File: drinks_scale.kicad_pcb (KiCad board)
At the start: 2 copper layers, 62.2 x 34.3 mm, 4 parts, among them J1 CONN_01X02, J2 CONN_01X04, U1 hx711, U2 WeMos_mini

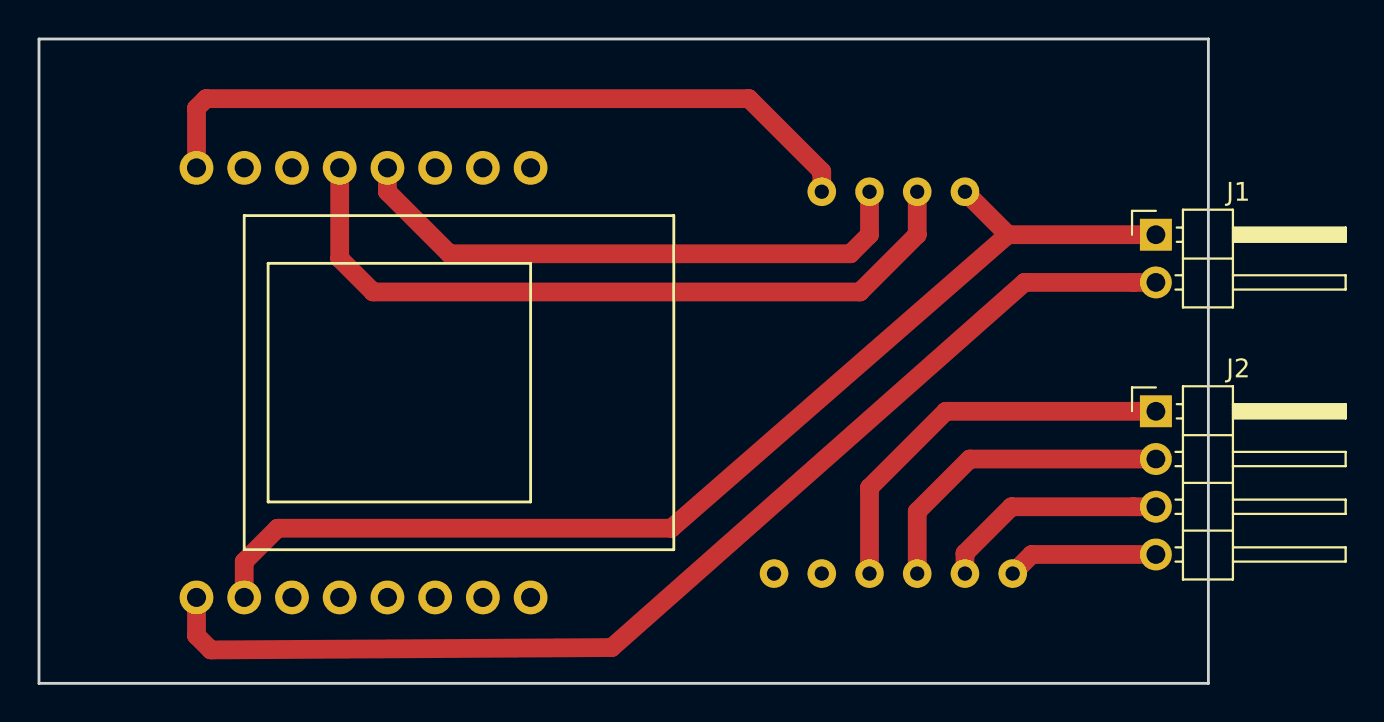
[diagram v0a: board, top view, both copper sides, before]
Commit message: Add GND plane
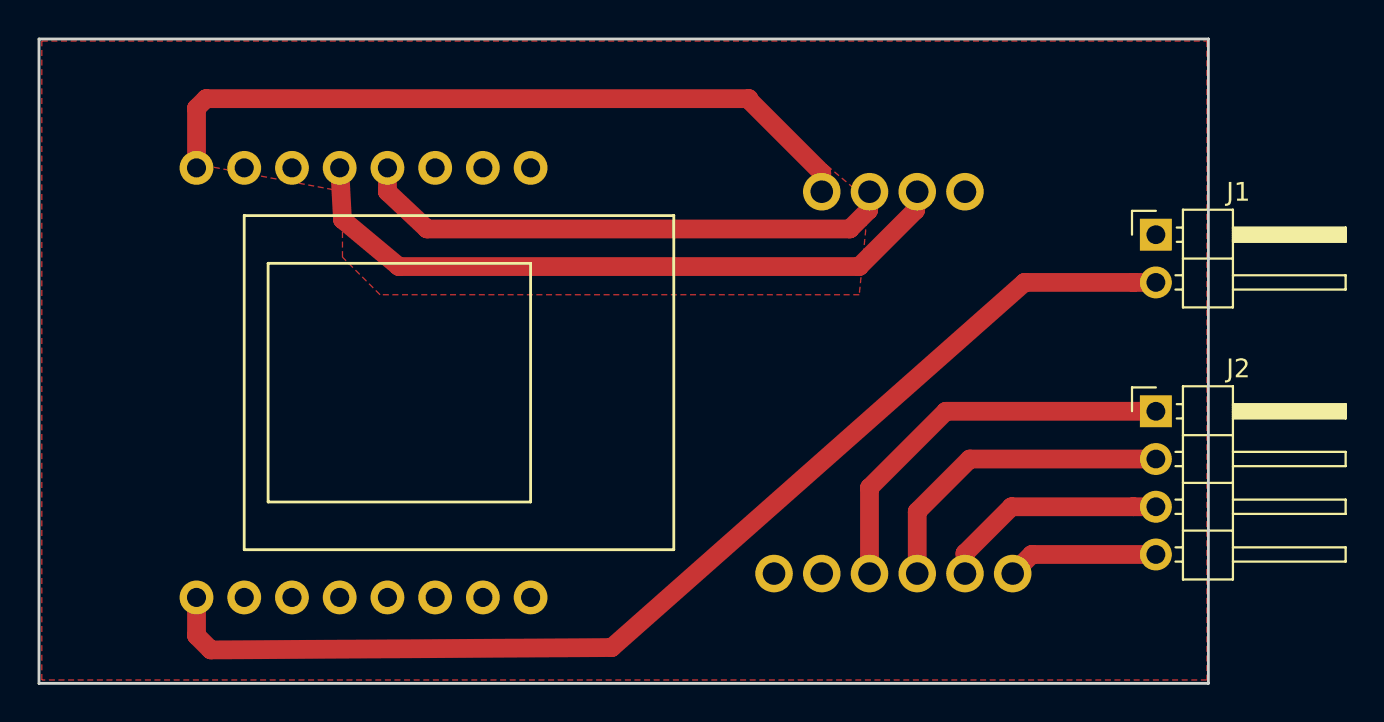
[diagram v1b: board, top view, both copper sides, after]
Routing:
- net GND: track 60.2 -> 0.00 mm
- net /data: track 39.8 -> 36.4 mm
- net /sck: track 31.0 -> 29.1 mm
- added copper zone on F.Cu, net (none)
- added copper zone on F.Cu, net GND
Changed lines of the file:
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@@
     (links 10)
     (no_connects 0)
-    (area 69.774999 72.314999 132.155001 106.755001)
+    (area 66.067 72.314999 140.061001 106.755001)
     (thickness 1.6)
     (drawings 4)
-    (tracks 39)
+    (tracks 34)
     (zones 0)
     (modules 4)
@@
     (trace_clearance 0.2)
     (zone_clearance 0.508)
-    (zone_45_only no)
+    (zone_45_only yes)
     (trace_min 0.2)
     (segment_width 0.2)
@@
     (fp_line (start -12.7 -10.16) (end 12.7 -10.16) (layer B.SilkS) (width 0.15))
     (fp_line (start -12.7 7.62) (end -12.7 -10.16) (layer B.SilkS) (width 0.15))
-    (pad 1 thru_hole circle (at -10.16 5.08 90) (size 1.524 1.524) (drill 0.762) (layers *.Cu *.Mask)
+    (pad 1 thru_hole circle (at -10.16 5.08 90) (size 2 2) (drill 1.2) (layers *.Cu *.Mask)
       (net 6 "Net-(J2-Pad4)"))
-    (pad 2 thru_hole circle (at -10.16 2.54 90) (size 1.524 1.524) (drill 0.762) (layers *.Cu *.Mask)
+    (pad 2 thru_hole circle (at -10.16 2.54 90) (size 2 2) (drill 1.2) (layers *.Cu *.Mask)
       (net 5 "Net-(J2-Pad3)"))
-    (pad 3 thru_hole circle (at -10.16 0 90) (size 1.524 1.524) (drill 0.762) (layers *.Cu *.Mask)
+    (pad 3 thru_hole circle (at -10.16 0 90) (size 2 2) (drill 1.2) (layers *.Cu *.Mask)
       (net 4 "Net-(J2-Pad2)"))
-    (pad 4 thru_hole circle (at -10.16 -2.54 90) (size 1.524 1.524) (drill 0.762) (layers *.Cu *.Mask)
+    (pad 4 thru_hole circle (at -10.16 -2.54 90) (size 2 2) (drill 1.2) (layers *.Cu *.Mask)
       (net 3 "Net-(J2-Pad1)"))
-    (pad 5 thru_hole circle (at -10.16 -5.08 90) (size 1.524 1.524) (drill 0.762) (layers *.Cu *.Mask))
-    (pad 6 thru_hole circle (at -10.16 -7.62 90) (size 1.524 1.524) (drill 0.762) (layers *.Cu *.Mask))
-    (pad 10 thru_hole circle (at 10.16 -5.08 90) (size 1.524 1.524) (drill 0.762) (layers *.Cu *.Mask)
+    (pad 5 thru_hole circle (at -10.16 -5.08 90) (size 2 2) (drill 1.2) (layers *.Cu *.Mask))
+    (pad 6 thru_hole circle (at -10.16 -7.62 90) (size 2 2) (drill 1.2) (layers *.Cu *.Mask))
+    (pad 10 thru_hole circle (at 10.16 -5.08 90) (size 2 2) (drill 1.2) (layers *.Cu *.Mask)
       (net 9 +3V3))
-    (pad 9 thru_hole circle (at 10.16 -2.54 90) (size 1.524 1.524) (drill 0.762) (layers *.Cu *.Mask)
+    (pad 9 thru_hole circle (at 10.16 -2.54 90) (size 2 2) (drill 1.2) (layers *.Cu *.Mask)
       (net 8 /sck))
-    (pad 8 thru_hole circle (at 10.16 0 90) (size 1.524 1.524) (drill 0.762) (layers *.Cu *.Mask)
+    (pad 8 thru_hole circle (at 10.16 0 90) (size 2 2) (drill 1.2) (layers *.Cu *.Mask)
       (net 7 /data))
-    (pad 7 thru_hole circle (at 10.16 2.54 90) (size 1.524 1.524) (drill 0.762) (layers *.Cu *.Mask)
+    (pad 7 thru_hole circle (at 10.16 2.54 90) (size 2 2) (drill 1.2) (layers *.Cu *.Mask)
       (net 1 GND))
   )
@@
   (gr_line (start 132.08 72.39) (end 132.08 106.68) (angle 90) (layer Edge.Cuts) (width 0.15))
   (gr_line (start 69.85 72.39) (end 132.08 72.39) (angle 90) (layer Edge.Cuts) (width 0.15))
-  (segment (start 121.412 82.804) (end 103.505 98.425) (width 1) (layer F.Cu) (net 1))
-  (segment (start 103.505 98.425) (end 82.55 98.425) (width 1) (layer F.Cu) (net 1))
-  (segment (start 82.55 98.425) (end 80.772 100.203) (width 1) (layer F.Cu) (net 1))
-  (segment (start 80.772 100.203) (end 80.772 102.108) (width 1) (layer F.Cu) (net 1))
-  (segment (start 119.126 80.518) (end 121.412 82.804) (width 1) (layer F.Cu) (net 1))
-  (segment (start 121.412 82.804) (end 129.286 82.804) (width 1) (layer F.Cu) (net 1))
   (segment (start 128.083919 85.344) (end 129.286 85.344) (width 1) (layer F.Cu) (net 2))
   (segment (start 78.232 102.108) (end 78.232 104.14) (width 1) (layer F.Cu) (net 2))
@@
   (segment (start 122.682 99.822) (end 129.286 99.822) (width 1) (layer F.Cu) (net 6))
   (segment (start 121.666 100.838) (end 122.682 99.822) (width 1) (layer F.Cu) (net 6))
-  (segment (start 85.852 79.248) (end 85.852 84.074) (width 1) (layer F.Cu) (net 7))
-  (segment (start 85.852 84.074) (end 87.63 85.852) (width 1) (layer F.Cu) (net 7))
-  (segment (start 87.63 85.852) (end 113.538 85.852) (width 1) (layer F.Cu) (net 7))
-  (segment (start 113.538 85.852) (end 116.586 82.804) (width 1) (layer F.Cu) (net 7))
-  (segment (start 116.586 82.804) (end 116.586 80.518) (width 1) (layer F.Cu) (net 7))
-  (segment (start 113.03 83.82) (end 114.046 82.804) (width 1) (layer F.Cu) (net 8))
-  (segment (start 114.046 82.804) (end 114.046 80.518) (width 1) (layer F.Cu) (net 8))
-  (segment (start 91.691208 83.82) (end 113.03 83.82) (width 1) (layer F.Cu) (net 8))
+  (segment (start 85.852 79.248) (end 86 82) (width 1) (layer F.Cu) (net 7) (status 400000))
+  (segment (start 86 82) (end 89 84.5) (width 1) (layer F.Cu) (net 7))
+  (segment (start 89 84.5) (end 113.5 84.5) (width 1) (layer F.Cu) (net 7))
+  (segment (start 113.5 84.5) (end 116.5 81.5) (width 1) (layer F.Cu) (net 7))
+  (segment (start 116.5 81.5) (end 116.586 80.518) (width 1) (layer F.Cu) (net 7) (status 800000))
+  (segment (start 113 82.5) (end 114 81.5) (width 1) (layer F.Cu) (net 8))
+  (segment (start 114 81.5) (end 114.046 80.518) (width 1) (layer F.Cu) (net 8) (status 800000))
+  (segment (start 90.5 82.5) (end 113 82.5) (width 1) (layer F.Cu) (net 8))
   (segment (start 88.392 79.248) (end 88.392 80.520792) (width 1) (layer F.Cu) (net 8))
-  (segment (start 88.392 80.520792) (end 91.691208 83.82) (width 1) (layer F.Cu) (net 8))
+  (segment (start 88.392 80.520792) (end 90.5 82.5) (width 1) (layer F.Cu) (net 8))
+  (segment (start 111.506 80.518) (end 111.506 79.506) (width 1) (layer F.Cu) (net 9))
+  (segment (start 78.74 75.565) (end 78.232 76.073) (width 1) (layer F.Cu) (net 9))
+  (segment (start 107.63063 75.565) (end 78.74 75.565) (width 1) (layer F.Cu) (net 9))
   (segment (start 78.232 76.073) (end 78.232 79.248) (width 1) (layer F.Cu) (net 9))
-  (segment (start 111.506 80.518) (end 111.506 79.44037) (width 1) (layer F.Cu) (net 9))
-  (segment (start 111.506 79.44037) (end 107.63063 75.565) (width 1) (layer F.Cu) (net 9))
-  (segment (start 107.63063 75.565) (end 78.74 75.565) (width 1) (layer F.Cu) (net 9))
-  (segment (start 78.74 75.565) (end 78.232 76.073) (width 1) (layer F.Cu) (net 9))
+  (segment (start 107.63063 75.565) (end 107.63063 75.63063) (width 1) (layer F.Cu) (net 9))
+  (segment (start 111.506 79.506) (end 107.63063 75.63063) (width 1) (layer F.Cu) (net 9))
+  (zone (net 1) (net_name GND) (layer F.Cu) (hatch edge 0.508)
+    (connect_pads (clearance 0.508))
+    (min_thickness 0.254)
+    (fill yes (arc_segments 16) (thermal_gap 0.508) (thermal_bridge_width 0.508) (smoothing fillet))
+    (polygon
+      (pts
+        (xy 132 106.5) (xy 70 106.5) (xy 70 72.5) (xy 132 72.5)
+      )
+    )
+  )
+  (zone (net 0) (net_name "") (layer F.Cu) (hatch edge 0.508)
+    (connect_pads (clearance 0.508))
+    (min_thickness 0.254)
+    (keepout (tracks not_allowed) (vias not_allowed) (copperpour not_allowed))
+    (fill yes (arc_segments 16) (thermal_gap 0.508) (thermal_bridge_width 0.508))
+    (polygon
+      (pts
+        (xy 96 85.5) (xy 96 97.5) (xy 104 97.5) (xy 104 85.5)
+      )
+    )
+  )
+  (zone (net 0) (net_name "") (layer F.Cu) (hatch full 0.508)
+    (connect_pads (clearance 0.508))
+    (min_thickness 0.254)
+    (fill yes (arc_segments 16) (thermal_gap 0.508) (thermal_bridge_width 0.508))
+    (polygon
+      (pts
+        (xy 113.5 86) (xy 88 86) (xy 86 84) (xy 86 80.5) (xy 78 79)
+        (xy 78 76.5) (xy 79 75.5) (xy 107.5 75.5) (xy 114 81)
+      )
+    )
+  )
 )
